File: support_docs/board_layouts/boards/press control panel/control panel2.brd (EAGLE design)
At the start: 93.7 x 69.9 mm, 21 parts, among them X1 009176002

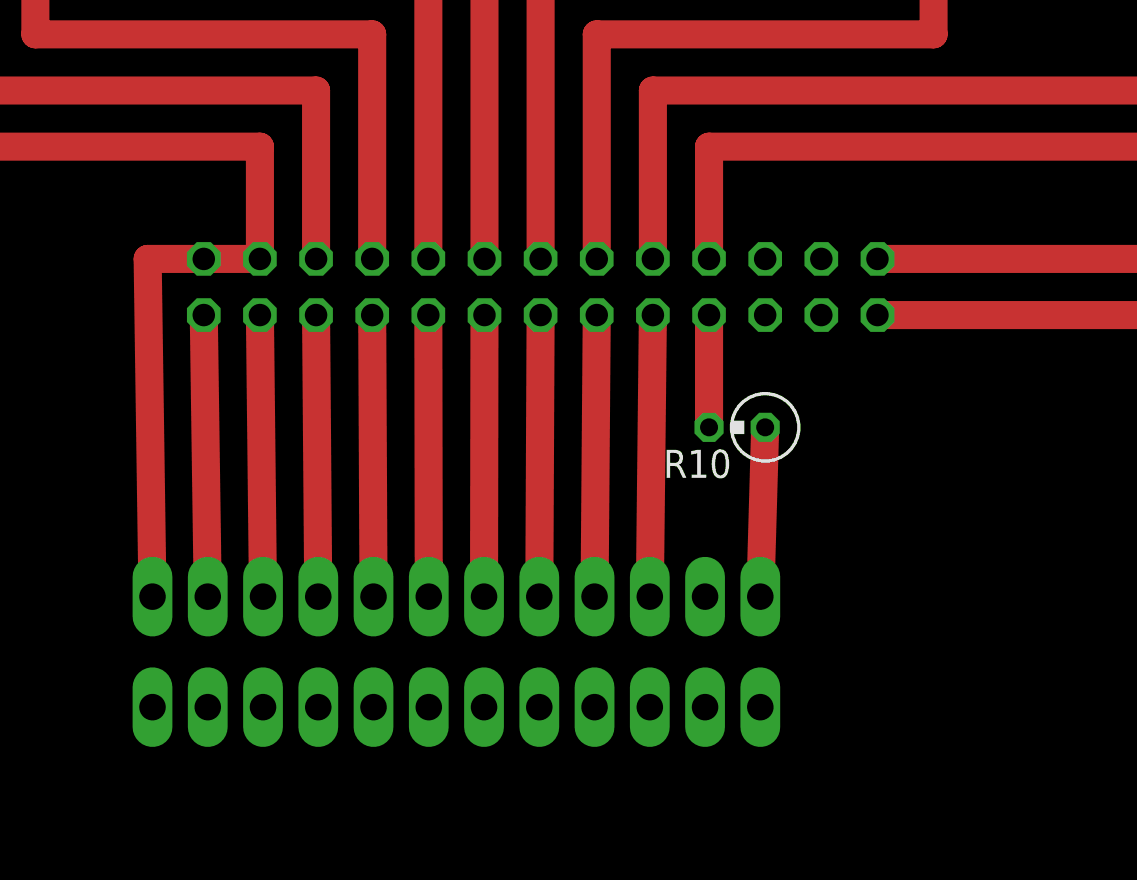
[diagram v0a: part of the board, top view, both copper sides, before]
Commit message: add led control
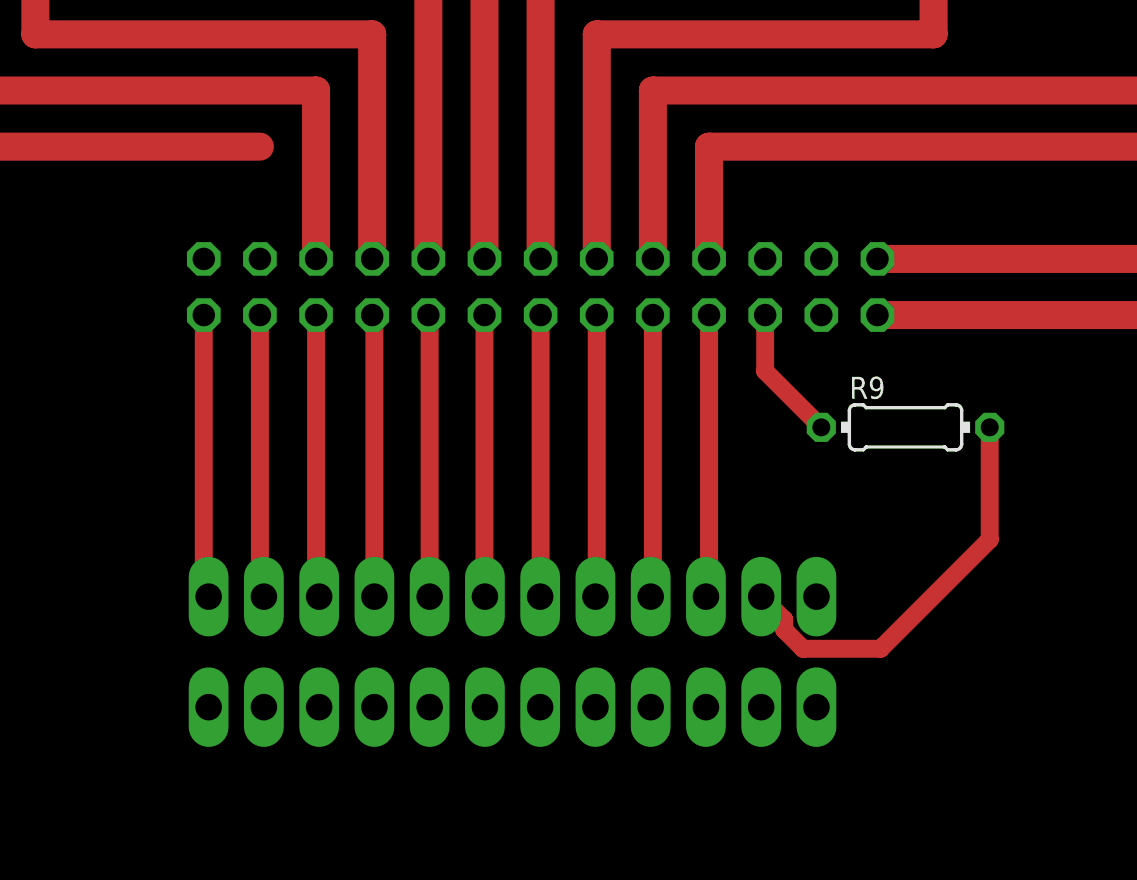
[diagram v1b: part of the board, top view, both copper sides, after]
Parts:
- removed R10: (no value), resistor:0309V
- added R9: (no value), resistor:0204/7
- moved X4 2.54 mm to (39.4, 33.0)
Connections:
- new net N$32: R9.2, X4.B11
- net GND: now also SV1.2; no longer SV1.1
- net N$17: now also SV1.24, X4.B12; no longer SV1.2, X4.B2
- net N$18: now also X4.B2; no longer X4.B3
- net N$19: now also X4.B3; no longer X4.B4
- net N$20: now also X4.B4; no longer X4.B5
- net N$21: now also X4.B5; no longer X4.B6
- net N$22: now also X4.B6; no longer X4.B7
- net N$23: now also X4.B7; no longer X4.B8
- net N$24: now also X4.B8; no longer X4.B9
- net N$27: now also X4.B9; no longer X4.B10
- net N$28: now also X4.B10; no longer R10.2
- net N$31: now also R9.1, SV1.22; no longer R10.1, X4.B12
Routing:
- net N$32: track 0.00 -> 18.7 mm
- net N$17: track 12.7 -> 0.00 mm
- net GND: track 147.4 -> 134.8 mm
- net N$28: track 5.08 -> 12.8 mm
- net N$22: track 12.7 -> 15.2 mm
- net N$31: track 7.66 -> 6.13 mm
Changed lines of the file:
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@@
 <?xml version="1.0" encoding="utf-8"?>
 <!DOCTYPE eagle SYSTEM "eagle.dtd">
-<eagle version="8.6.3">
+<eagle version="8.7.0">
 <drawing>
 <settings>
@@
 <attribute name="OC_NEWARK" value="66M1960" x="83.82" y="49.53" size="1.778" layer="27" rot="R90" display="off"/>
 </element>
-<element name="X4" library="con-wago" library_urn="urn:adsk.eagle:library:197" package="233-212" value="" x="36.83" y="33.02" rot="MR180">
-<attribute name="MF" value="" x="36.83" y="33.02" size="1.778" layer="28" rot="MR180" display="off"/>
-<attribute name="MPN" value="233-212" x="36.83" y="33.02" size="1.778" layer="28" rot="MR180" display="off"/>
-<attribute name="OC_FARNELL" value="1283538" x="36.83" y="33.02" size="1.778" layer="28" rot="MR180" display="off"/>
-<attribute name="OC_NEWARK" value="28K9068" x="36.83" y="33.02" size="1.778" layer="28" rot="MR180" display="off"/>
+<element name="X4" library="con-wago" library_urn="urn:adsk.eagle:library:197" package="233-212" value="" x="39.37" y="33.02" rot="MR180">
+<attribute name="MF" value="" x="39.37" y="33.02" size="1.778" layer="28" rot="MR180" display="off"/>
+<attribute name="MPN" value="233-212" x="39.37" y="33.02" size="1.778" layer="28" rot="MR180" display="off"/>
+<attribute name="OC_FARNELL" value="1283538" x="39.37" y="33.02" size="1.778" layer="28" rot="MR180" display="off"/>
+<attribute name="OC_NEWARK" value="28K9068" x="39.37" y="33.02" size="1.778" layer="28" rot="MR180" display="off"/>
 </element>
-<element name="R10" library="resistor" library_urn="urn:adsk.eagle:library:348" package="0309V" package3d_urn="urn:adsk.eagle:package:26090/1" value="" x="49.53" y="43.18" rot="R180"/>
+<element name="R9" library="resistor" library_urn="urn:adsk.eagle:library:348" package="0204/7" package3d_urn="urn:adsk.eagle:package:25945/1" value="" x="57.15" y="43.18"/>
 </elements>
 <signals>
@@
 <wire x1="7.62" y1="76.2" x2="2.54" y2="76.2" width="1.27" layer="1"/>
 <wire x1="2.54" y1="55.88" x2="2.54" y2="76.2" width="1.27" layer="1"/>
+<wire x1="27.94" y1="55.88" x2="2.54" y2="55.88" width="1.27" layer="1"/>
+<contactref element="SV1" pad="2"/>
+<contactref element="X4" pad="B1"/>
 <contactref element="SV1" pad="3"/>
-<wire x1="27.94" y1="50.8" x2="27.94" y2="55.88" width="1.27" layer="1"/>
-<wire x1="27.94" y1="55.88" x2="2.54" y2="55.88" width="1.27" layer="1"/>
-<contactref element="SV1" pad="1"/>
-<wire x1="27.94" y1="50.8" x2="25.4" y2="50.8" width="1.27" layer="1"/>
-<contactref element="X4" pad="B1"/>
-<wire x1="25.4" y1="50.8" x2="22.86" y2="50.8" width="1.27" layer="1"/>
-<wire x1="22.86" y1="50.8" x2="23.08" y2="35.52" width="1.27" layer="1"/>
+<wire x1="25.49" y1="35.65" x2="25.62" y2="35.52" width="0.1524" layer="1"/>
+<wire x1="25.4" y1="48.26" x2="25.4" y2="35.74" width="0.8128" layer="1"/>
+<wire x1="25.4" y1="35.74" x2="25.49" y2="35.65" width="0.8128" layer="1"/>
+<wire x1="25.4" y1="48.26" x2="27.94" y2="50.8" width="0" layer="19" extent="1-1"/>
+<wire x1="27.94" y1="55.88" x2="27.94" y2="50.8" width="0" layer="19" extent="1-1"/>
 </signal>
 <signal name="N$25">
@@
 <contactref element="LED9" pad="A"/>
 </signal>
+<signal name="N$18">
+<contactref element="X4" pad="B2"/>
+<contactref element="SV1" pad="4"/>
+<wire x1="27.94" y1="48.26" x2="27.94" y2="35.7" width="0.8128" layer="1"/>
+<wire x1="27.94" y1="35.7" x2="28.12" y2="35.52" width="0.8128" layer="1"/>
+</signal>
+<signal name="N$19">
+<contactref element="X4" pad="B3"/>
+<contactref element="SV1" pad="6"/>
+<wire x1="30.48" y1="48.26" x2="30.48" y2="35.56" width="0.8128" layer="1"/>
+<wire x1="30.48" y1="35.56" x2="30.52" y2="35.52" width="0.8128" layer="1"/>
+<wire x1="30.52" y1="35.52" x2="30.62" y2="35.52" width="0.8128" layer="1"/>
+</signal>
+<signal name="N$20">
+<contactref element="X4" pad="B4"/>
+<contactref element="SV1" pad="8"/>
+<wire x1="33.02" y1="48.26" x2="33.12" y2="48.16" width="0.8128" layer="1"/>
+<wire x1="33.12" y1="48.16" x2="33.12" y2="35.52" width="0.8128" layer="1"/>
+</signal>
+<signal name="N$21">
+<contactref element="X4" pad="B5"/>
+<contactref element="SV1" pad="10"/>
+<wire x1="35.56" y1="48.26" x2="35.62" y2="48.2" width="0.8128" layer="1"/>
+<wire x1="35.62" y1="48.2" x2="35.62" y2="35.52" width="0.8128" layer="1"/>
+</signal>
+<signal name="N$22">
+<contactref element="X4" pad="B6"/>
+<contactref element="SV1" pad="12"/>
+<wire x1="38.1" y1="48.26" x2="38.1" y2="34.29" width="0.8128" layer="1"/>
+<wire x1="38.1" y1="34.29" x2="38.12" y2="34.31" width="0.8128" layer="1"/>
+<wire x1="38.12" y1="34.31" x2="38.12" y2="35.52" width="0.8128" layer="1"/>
+</signal>
+<signal name="N$23">
+<contactref element="X4" pad="B7"/>
+<contactref element="SV1" pad="14"/>
+<wire x1="40.64" y1="48.26" x2="40.64" y2="35.54" width="0.8128" layer="1"/>
+<wire x1="40.64" y1="35.54" x2="40.62" y2="35.52" width="0.8128" layer="1"/>
+</signal>
+<signal name="N$24">
+<contactref element="X4" pad="B8"/>
+<contactref element="SV1" pad="16"/>
+<wire x1="43.18" y1="48.26" x2="43.18" y2="35.58" width="0.8128" layer="1"/>
+<wire x1="43.18" y1="35.58" x2="43.12" y2="35.52" width="0.8128" layer="1"/>
+</signal>
+<signal name="N$27">
+<contactref element="X4" pad="B9"/>
+<contactref element="SV1" pad="18"/>
+<wire x1="45.72" y1="48.26" x2="45.72" y2="35.62" width="0.8128" layer="1"/>
+<wire x1="45.72" y1="35.62" x2="45.62" y2="35.52" width="0.8128" layer="1"/>
+</signal>
+<signal name="N$28">
+<contactref element="X4" pad="B10"/>
+<contactref element="SV1" pad="20"/>
+<wire x1="48.26" y1="48.26" x2="48.26" y2="35.66" width="0.8128" layer="1"/>
+<wire x1="48.26" y1="35.66" x2="48.12" y2="35.52" width="0.8128" layer="1"/>
+</signal>
+<signal name="N$31">
+<contactref element="SV1" pad="22"/>
+<contactref element="R9" pad="1"/>
+<wire x1="50.8" y1="48.26" x2="50.8" y2="45.72" width="0.8128" layer="1"/>
+<wire x1="50.8" y1="45.72" x2="53.34" y2="43.18" width="0.8128" layer="1"/>
+</signal>
+<signal name="N$32">
+<contactref element="X4" pad="B11"/>
+<contactref element="R9" pad="2"/>
+<wire x1="60.96" y1="43.18" x2="60.96" y2="38.1" width="0.8128" layer="1"/>
+<wire x1="52.51574375" y1="33.1612" x2="51.6612" y2="34.01574375" width="0.8128" layer="1"/>
+<wire x1="51.6612" y1="34.01574375" x2="51.6612" y2="34.4788" width="0.8128" layer="1"/>
+<wire x1="51.6612" y1="34.4788" x2="50.62" y2="35.52" width="0.8128" layer="1"/>
+<wire x1="56.0212" y1="33.1612" x2="52.51574375" y2="33.1612" width="0.8128" layer="1"/>
+<wire x1="60.96" y1="38.1" x2="56.0212" y2="33.1612" width="0.8128" layer="1"/>
+</signal>
 <signal name="N$17">
-<contactref element="SV1" pad="2"/>
-<contactref element="X4" pad="B2"/>
-<wire x1="25.4" y1="48.26" x2="25.58" y2="35.52" width="1.27" layer="1"/>
-</signal>
-<signal name="N$18">
-<contactref element="SV1" pad="4"/>
-<contactref element="X4" pad="B3"/>
-<wire x1="27.94" y1="48.26" x2="28.08" y2="35.52" width="1.27" layer="1"/>
-</signal>
-<signal name="N$19">
-<contactref element="SV1" pad="6"/>
-<contactref element="X4" pad="B4"/>
-<wire x1="30.48" y1="48.26" x2="30.58" y2="35.52" width="1.27" layer="1"/>
-</signal>
-<signal name="N$20">
-<contactref element="SV1" pad="8"/>
-<contactref element="X4" pad="B5"/>
-<wire x1="33.02" y1="48.26" x2="33.08" y2="35.52" width="1.27" layer="1"/>
-</signal>
-<signal name="N$21">
-<contactref element="SV1" pad="10"/>
-<contactref element="X4" pad="B6"/>
-<wire x1="35.56" y1="48.26" x2="35.58" y2="35.52" width="1.27" layer="1"/>
-</signal>
-<signal name="N$22">
-<contactref element="SV1" pad="12"/>
-<contactref element="X4" pad="B7"/>
-<wire x1="38.1" y1="48.26" x2="38.08" y2="35.52" width="1.27" layer="1"/>
-</signal>
-<signal name="N$23">
-<contactref element="SV1" pad="14"/>
-<contactref element="X4" pad="B8"/>
-<wire x1="40.64" y1="48.26" x2="40.58" y2="35.52" width="1.27" layer="1"/>
-</signal>
-<signal name="N$24">
-<contactref element="SV1" pad="16"/>
-<contactref element="X4" pad="B9"/>
-<wire x1="43.18" y1="48.26" x2="43.08" y2="35.52" width="1.27" layer="1"/>
-</signal>
-<signal name="N$27">
-<contactref element="SV1" pad="18"/>
-<contactref element="X4" pad="B10"/>
-<wire x1="45.72" y1="48.26" x2="45.58" y2="35.52" width="1.27" layer="1"/>
-</signal>
-<signal name="N$28">
-<contactref element="SV1" pad="20"/>
-<contactref element="R10" pad="2"/>
-<wire x1="48.26" y1="48.26" x2="48.26" y2="43.18" width="1.27" layer="1"/>
-</signal>
-<signal name="N$31">
-<contactref element="R10" pad="1"/>
+<contactref element="SV1" pad="24"/>
 <contactref element="X4" pad="B12"/>
-<wire x1="50.8" y1="43.18" x2="50.58" y2="35.52" width="1.27" layer="1"/>
+<wire x1="53.12" y1="35.52" x2="53.34" y2="48.26" width="0" layer="19" extent="1-1"/>
 </signal>
 </signals>
